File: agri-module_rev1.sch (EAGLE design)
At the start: 0 parts

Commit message: add ISL and new RJ45 pinout
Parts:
- added C1, C2: 100nF, BrainGrid - Capacitors:C_100N_0402
- added LED1, LED2, LED3: (no value), BrainGrid - Diodes:LEDCHIPLED-0603-TTW
- added R1, R2: 1.8k, BrainGrid - Resistors:R_1.8K_0402
- added U$1: RJ45_RA_SMD, BrainGrid - Electromechanical:RJ45_RA_SMD
- added U$2: RJ45_OUT_AGRI-BRD, BrainGrid - Electromechanical:RJ45_OUT_AGRI-BRD
- added U$3: BME280, BrainGrid - Sensors:BME280
- added U$4: ADS1015, BrainGrid - Analog:ADS1015
- added U$5: ISL29125_RGB_SENSE, BrainGrid - Sensors:ISL29125_RGB_SENSE
- added U$6: PCA9540B_I2C_SWITCH, NXP:PCA9540B_I2C_SWITCH
- added U1: 74HC1G79GW, NXP:74HC1G79GW
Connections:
- new net 3.6V_HP: C1.1, C2.1, R1.2, R2.2, U$1.+5V', U$3.CSB, U$3.VCC, U$3.VREF, U$4.ADDR, U$4.VCC, U$6.VCC
- new net 5V: U$1.+5V, U$2.+5V
- new net GND: LED1.C, LED2.C, LED3.C, U$1.GND, U$2.GND, U$3.GND1, U$4.GND, U$6.GND
- new net N$1: R1.1, U$3.SDI
- new net N$10: U$1.GND'
- new net N$11: U$1.SDA, U$6.SDA
- new net N$12: U$3.SDO, U$4.SDA, U$5.SDA, U$6.D0
- new net N$13: U$3.SCK, U$4.SCL, U$5.SCL, U$6.C0
- new net N$14: C1.2, C2.2, U$3.GND2
- new net N$2: R2.1
- new net N$3: U$1.SCL, U$6.SCL
- new net N$4: U$4.CH0
- new net N$5: LED3.A, U$4.CH1
- new net N$6: LED2.A, U$4.CH2
- new net N$7: LED1.A, U$4.CH3
- new net N$8: U$6.C1
- new net N$9: U$6.D1
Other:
- note added: "ADD CO2"
- note added: "ADD PULLUPS"
- note added: "CHAIN DIRECTION"
- note added: "Spectra ADC"

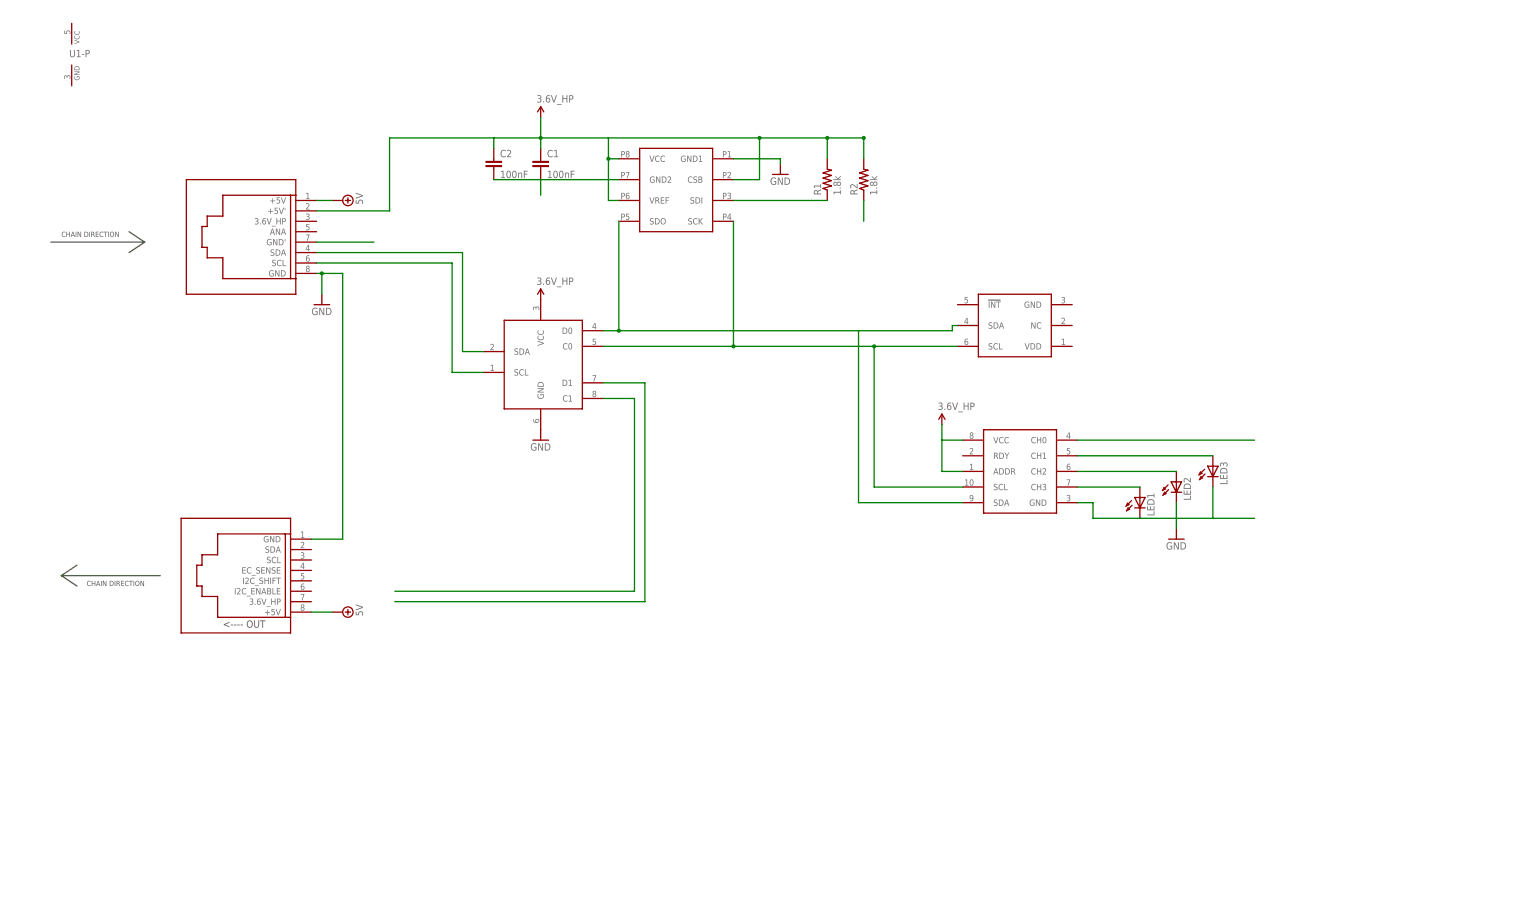
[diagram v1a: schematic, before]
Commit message: Everything wired up, not looked over yet
-replaced ISL with RGB gesture
-added hot film amp and CO2 amp
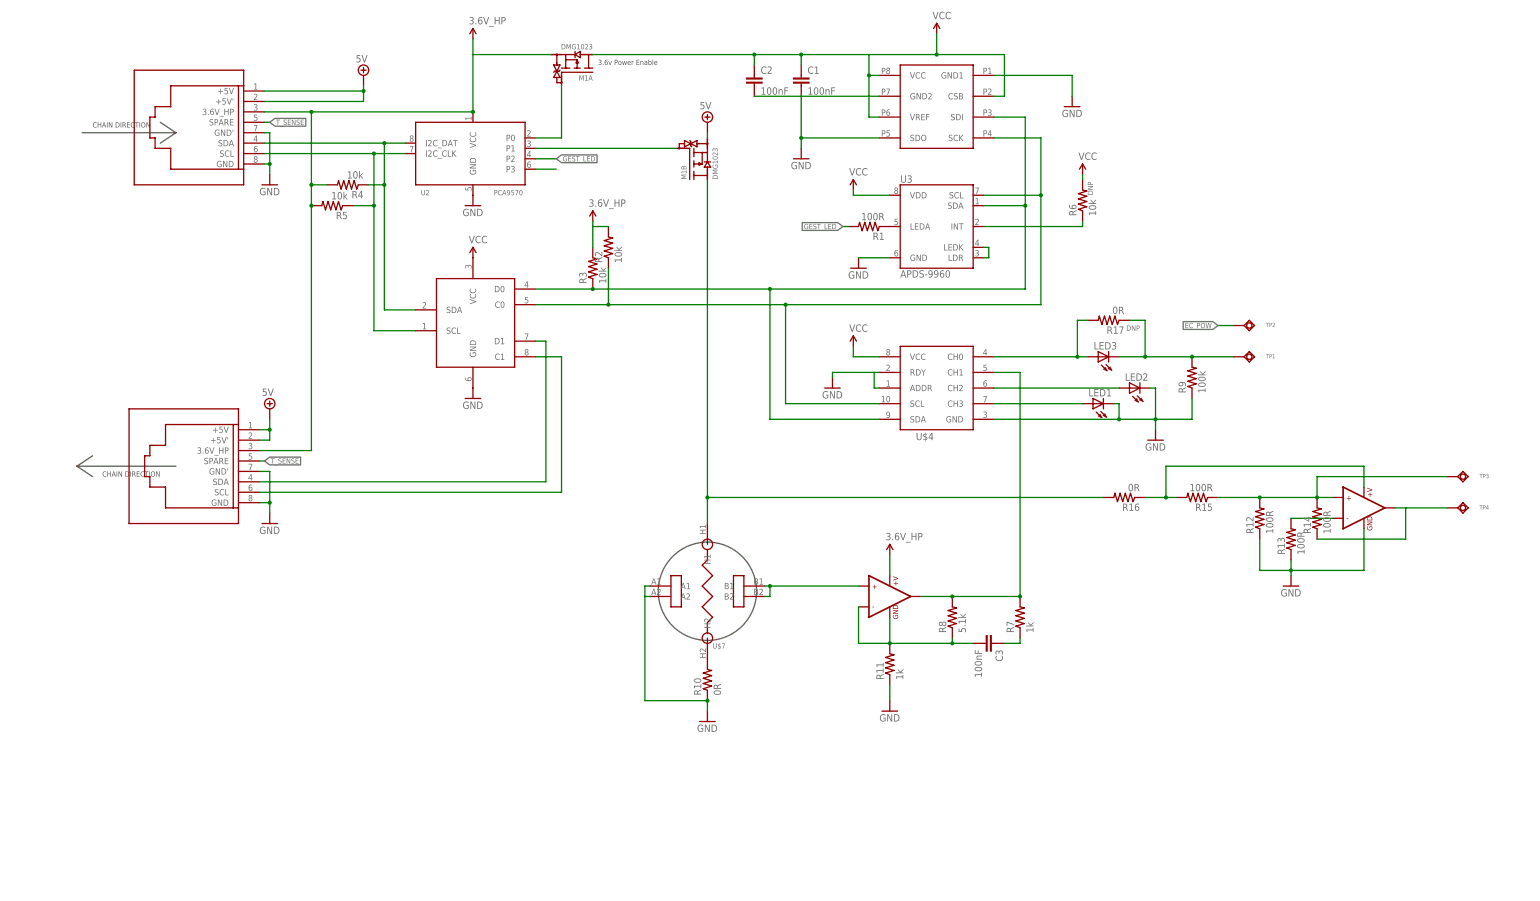
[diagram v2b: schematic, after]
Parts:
- removed U1: 74HC1G79GW, NXP:74HC1G79GW
- added C3: 100nF, BrainGrid - Capacitors:C_100N_0402
- added M1: DMG1023, BrainGrid - Transistors:DMG1023
- added R10, R16, R17: 0R, BrainGrid - Resistors:R_0R_0402
- added R11, R7: 1k, BrainGrid - Resistors:R_1K_0402
- added R12, R13, R14, R15: 100R, BrainGrid - Resistors:R_100R_0402
- added R3, R4, R5, R6: 10k, BrainGrid - Resistors:R_10K_0402
- added R8: 5.1k, BrainGrid - Resistors:R_5.1K_0402
- added R9: 100k, BrainGrid - Resistors:R_100K_0402
- added TP1, TP2, TP3, TP4: TEST_PAD, BrainGrid - Electromechanical:TEST_PAD
- added U$7: MG811, BrainGrid - Sensors:MG811
- added U$8: MCP6001T, SparkFun-AnalogIC:MCP6001T
- added U2: PCA9570, BrainGrid - MAC-PHY-Glue:PCA9570
- added U3: APDS-9960, BrainGrid - Sensors:APDS-9960
- R1: value 1.8k -> 100R; device BrainGrid - Resistors:R_1.8K_0402 -> BrainGrid - Resistors:R_100R_0402
- R2: value 1.8k -> 10k; device BrainGrid - Resistors:R_1.8K_0402 -> BrainGrid - Resistors:R_10K_0402
- U$2: value RJ45_OUT_AGRI-BRD -> RJ45_RA_SMD; device BrainGrid - Electromechanical:RJ45_OUT_AGRI-BRD -> BrainGrid - Electromechanical:RJ45_RA_SMD
- U$5: value ISL29125_RGB_SENSE -> MCP6001T; device BrainGrid - Sensors:ISL29125_RGB_SENSE -> SparkFun-AnalogIC:MCP6001T
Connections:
- removed net N$5 (its old number): LED3.A, U$4.CH1
- new net CO2_POW: M1B.D2, R16.2, U$7.H1
- new net EC_POW: TP2.TP, U2.P3
- new net GEST_LED: R1.2, U2.P2
- new net N$15: R5.1, U$1.SCL, U$6.SCL, U2.I2C_CLK
- new net N$16: R7.2, R8.2, U$4.CH1, U$5.OUT1
- new net N$17: R10.2, U$7.H2
- new net N$18: M1B.G2, U2.P1
- new net N$19: C3.1, R7.1
- new net N$20: R13.2, U$8.-IN1
- new net N$21: R12.2, R14.2, R15.1, TP3.TP, U$8.+IN1
- new net N$22: R14.1, TP4.TP, U$8.OUT1
- new net N$23: R15.2, R16.1, U$8.+V
- new net N$24: LED3.A, R17.2, U$4.CH0
- new net N$7: U$2.SDA, U$6.D1
- new net T_SENSE: U$1.SPARE, U$2.SPARE
- new net VCC: C1.1, C2.1, M1A.D2, R6.2, U$3.CSB, U$3.VCC, U$3.VREF, U$4.VCC, U$6.VCC, U3.VDD
- net 3.6V_HP: now also M1A.S2, R3.2, R4.2, R5.2, U$1.3.6V_HP, U$2.3.6V_HP, U$5.+V, U2.VCC; no longer C1.1, C2.1, R1.2, U$1.+5V', U$3.CSB, U$3.VCC, U$3.VREF, U$4.ADDR, U$4.VCC, U$6.VCC
- net 5V: now also M1B.S2, U$1.+5V', U$2.+5V'
- net GND: now also C1.2, C2.2, R10.1, R11.1, R12.1, R13.1, R9.1, U$1.GND', U$2.GND', U$3.GND2, U$3.SDO, U$4.ADDR, U$4.RDY, U$7.A1, U$7.A2, U$8.GND, U2.GND, U3.GND; no longer LED3.C
- net N$1: now also M1A.G2, U2.P0; no longer R1.1, U$3.SDI
- net N$10: now also R6.1, U3.INT; no longer U$1.GND'
- net N$11: now also R3.1, U$3.SDI, U$4.SDA, U$6.D0, U3.SDA; no longer U$1.SDA, U$6.SDA
- net N$12: now also LED3.C, R17.1, R9.2, TP1.TP; no longer U$3.SDO, U$4.SDA, U$5.SDA, U$6.D0
- net N$13: now also C3.2, R11.2, R8.1, U$5.-IN1, U$5.GND; no longer U$3.SCK, U$4.SCL, U$5.SCL, U$6.C0
- net N$14: now also R4.1, U$1.SDA, U$6.SDA, U2.I2C_DAT; no longer C1.2, C2.2, U$3.GND2
- net N$2: now also U3.LDR, U3.LEDK; no longer R2.1
- net N$3: now also R2.1, U$3.SCK, U$4.SCL, U$6.C0, U3.SCL; no longer U$1.SCL, U$6.SCL
- net N$4: now also R1.1, U3.LEDA; no longer U$4.CH0
- net N$8: now also U$2.SCL
- net N$9: now also U$5.+IN1, U$7.B1, U$7.B2; no longer U$6.D1
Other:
- note added: "3.6v Power Enable"
- note added: "adc-Mplex"
- note added: "check val"
- note added: "check vals"
- note added: "hot film"
- note added: "spectra i2c / gesture"
- note added: "temp/press/ humidity"
- note removed: "ADD CO2"
- note removed: "ADD PULLUPS"
- note removed: "Spectra ADC"
- moved on the sheet: C1, C2, LED1, LED2, LED3, R1, R2

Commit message: Added indication use for one of LEDs
-also connected EC_pow correctly
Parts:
- added D1: DB2S205, EAP - Library:DB2S205
- added R18: 10k, BrainGrid - Resistors:R_10K_0402
- added R19: 100R, BrainGrid - Resistors:R_100R_0402
- R1: value 100R -> 10k; device BrainGrid - Resistors:R_100R_0402 -> BrainGrid - Resistors:R_10K_0402
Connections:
- removed net N$6: LED2.A, U$4.CH2
- new net LED_INDICATE: D1.C, LED2.A, U$4.CH2
- net 3.6V_HP: now also R1.1, R18.1
- net GEST_LED: now also R19.2, U3.LEDA; no longer R1.2
- net N$4: now also D1.A, R19.1; no longer R1.1, U3.LEDA
- net N$7: now also R18.2
- net N$8: now also R1.2
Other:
- note removed: "check val"
- note removed: "check vals"
- moved on the sheet: R1
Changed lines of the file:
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@@
 <part name="GND4" library="BrainGrid - Supplies" deviceset="GND" device=""/>
 <part name="GND6" library="BrainGrid - Supplies" deviceset="GND" device=""/>
-<part name="R1" library="BrainGrid - Resistors" deviceset="R_100R" device="_0402" value="100R"/>
 <part name="R3" library="BrainGrid - Resistors" deviceset="R_10K" device="_0402" value="10k"/>
 <part name="SUPPLY2" library="BrainGrid - Supplies" deviceset="3.6V_HP" device=""/>
@@
 <attribute name="POPULATE" value="DNP"/>
 </part>
+<part name="R19" library="BrainGrid - Resistors" deviceset="R_100R" device="_0402" value="100R">
+<attribute name="POPULATE" value="DNP"/>
+</part>
+<part name="D1" library="EAP - Library" deviceset="DB2S205" device="">
+<attribute name="POPULATE" value="DNP"/>
+</part>
+<part name="R1" library="BrainGrid - Resistors" deviceset="R_10K" device="_0402" value="10k"/>
+<part name="R18" library="BrainGrid - Resistors" deviceset="R_10K" device="_0402" value="10k"/>
 </parts>
 <sheets>
@@
 <wire x1="26.67" y1="115.57" x2="30.48" y2="118.11" width="0.1524" layer="97"/>
 <text x="46.99" y="114.3" size="1.27" layer="97" rot="R180">CHAIN DIRECTION</text>
-<text x="210.82" y="176.53" size="1.27" layer="134">check val</text>
 <text x="229.87" y="176.53" size="0.8128" layer="90">spectra i2c
   / gesture</text>
@@
 humidity</text>
 <text x="233.68" y="128.27" size="0.8128" layer="90">adc-Mplex</text>
-<text x="157.48" y="162.56" size="1.27" layer="134">check vals</text>
-<text x="93.98" y="176.53" size="1.27" layer="134">check vals</text>
 <text x="356.87" y="107.95" size="1.27" layer="90">hot film</text>
 </plain>
@@
 <instance part="GND4" gate="G$1" x="123.19" y="132.08"/>
 <instance part="GND6" gate="G$1" x="123.19" y="179.07"/>
-<instance part="R1" gate="G$1" x="219.71" y="173.99" rot="R180"/>
 <instance part="R3" gate="G$1" x="152.4" y="163.83" rot="R90"/>
 <instance part="SUPPLY2" gate="G$1" x="152.4" y="175.26"/>
@@
 <attribute name="POPULATE" x="285.75" y="149.86" size="1.27" layer="96" rot="R180"/>
 </instance>
+<instance part="R19" gate="G$1" x="257.81" y="147.32" rot="R180">
+<attribute name="POPULATE" x="256.54" y="146.05" size="1.27" layer="96" rot="R180"/>
+</instance>
+<instance part="D1" gate="D" x="264.16" y="138.43" rot="R270">
+<attribute name="POPULATE" x="265.43" y="139.7" size="1.27" layer="96" rot="R270"/>
+</instance>
+<instance part="R1" gate="G$1" x="96.52" y="114.3" rot="R270"/>
+<instance part="R18" gate="G$1" x="104.14" y="116.84" rot="R270"/>
 </instances>
 <busses>
@@
 <pinref part="U$2" gate="G$1" pin="3.6V_HP"/>
 <wire x1="71.12" y1="119.38" x2="83.82" y2="119.38" width="0.1524" layer="91"/>
-<wire x1="83.82" y1="119.38" x2="83.82" y2="179.07" width="0.1524" layer="91"/>
 <junction x="83.82" y="179.07"/>
 <pinref part="SUPPLY1" gate="G$1" pin="3.6V_HP"/>
+<wire x1="83.82" y1="119.38" x2="83.82" y2="127" width="0.1524" layer="91"/>
+<wire x1="83.82" y1="127" x2="83.82" y2="179.07" width="0.1524" layer="91"/>
 <wire x1="123.19" y1="215.9" x2="123.19" y2="219.71" width="0.1524" layer="91"/>
+<pinref part="R18" gate="G$1" pin="1"/>
+<wire x1="96.52" y1="121.92" x2="100.33" y2="121.92" width="0.1524" layer="91"/>
+<pinref part="R1" gate="G$1" pin="1"/>
+<wire x1="100.33" y1="121.92" x2="104.14" y2="121.92" width="0.1524" layer="91"/>
+<wire x1="96.52" y1="119.38" x2="96.52" y2="121.92" width="0.1524" layer="91"/>
+<wire x1="100.33" y1="121.92" x2="100.33" y2="127" width="0.1524" layer="91"/>
+<wire x1="100.33" y1="127" x2="83.82" y2="127" width="0.1524" layer="91"/>
+<junction x="83.82" y="127"/>
 </segment>
 <segment>
@@
 <net name="EC_POW" class="0">
 <segment>
-<pinref part="U2" gate="G$1" pin="P3"/>
-<wire x1="138.43" y1="187.96" x2="143.51" y2="187.96" width="0.1524" layer="91"/>
-</segment>
-<segment>
 <pinref part="TP2" gate="TP" pin="TP"/>
 <wire x1="308.61" y1="149.86" x2="304.8" y2="149.86" width="0.1524" layer="91"/>
 <label x="304.8" y="149.86" size="1.27" layer="95" rot="R180" xref="yes"/>
+</segment>
+<segment>
+<pinref part="U2" gate="G$1" pin="P3"/>
+<wire x1="138.43" y1="187.96" x2="143.51" y2="187.96" width="0.1524" layer="91"/>
+<label x="143.51" y="187.96" size="1.27" layer="95" xref="yes"/>
 </segment>
 </net>
@@
 </segment>
 </net>
-<net name="N$4" class="0">
-<segment>
-<pinref part="U3" gate="U" pin="LEDA"/>
-<pinref part="R1" gate="G$1" pin="1"/>
-</segment>
-</net>
 <net name="N$5" class="0">
 <segment>
@@
 </segment>
 </net>
-<net name="N$6" class="0">
+<net name="LED_INDICATE" class="0">
 <segment>
 <pinref part="U$4" gate="G$1" pin="CH2"/>
 <pinref part="LED2" gate="G$1" pin="A"/>
-<wire x1="250.19" y1="134.62" x2="280.67" y2="134.62" width="0.1524" layer="91"/>
+<wire x1="250.19" y1="134.62" x2="264.16" y2="134.62" width="0.1524" layer="91"/>
+<pinref part="D1" gate="D" pin="C"/>
+<wire x1="264.16" y1="134.62" x2="280.67" y2="134.62" width="0.1524" layer="91"/>
+<wire x1="264.16" y1="135.89" x2="264.16" y2="134.62" width="0.1524" layer="91"/>
+<junction x="264.16" y="134.62"/>
 </segment>
 </net>
@@
 <pinref part="U$2" gate="G$1" pin="SCL"/>
 <pinref part="U$6" gate="G$1" pin="C1"/>
-<wire x1="144.78" y1="109.22" x2="71.12" y2="109.22" width="0.1524" layer="91"/>
+<wire x1="144.78" y1="109.22" x2="96.52" y2="109.22" width="0.1524" layer="91"/>
+<wire x1="96.52" y1="109.22" x2="71.12" y2="109.22" width="0.1524" layer="91"/>
 <wire x1="138.43" y1="142.24" x2="144.78" y2="142.24" width="0.1524" layer="91"/>
 <wire x1="144.78" y1="142.24" x2="144.78" y2="109.22" width="0.1524" layer="91"/>
+<pinref part="R1" gate="G$1" pin="2"/>
+<junction x="96.52" y="109.22"/>
 </segment>
 </net>
@@
 <wire x1="140.97" y1="146.05" x2="140.97" y2="111.76" width="0.1524" layer="91"/>
 <pinref part="U$2" gate="G$1" pin="SDA"/>
-<wire x1="140.97" y1="111.76" x2="71.12" y2="111.76" width="0.1524" layer="91"/>
+<wire x1="140.97" y1="111.76" x2="104.14" y2="111.76" width="0.1524" layer="91"/>
+<pinref part="R18" gate="G$1" pin="2"/>
+<wire x1="104.14" y1="111.76" x2="71.12" y2="111.76" width="0.1524" layer="91"/>
+<junction x="104.14" y="111.76"/>
 </segment>
 </net>
@@
 </segment>
 <segment>
-<pinref part="R1" gate="G$1" pin="2"/>
-<wire x1="214.63" y1="173.99" x2="213.36" y2="173.99" width="0.1524" layer="91"/>
 <label x="213.36" y="173.99" size="1.27" layer="95" rot="R180" xref="yes"/>
+<pinref part="U3" gate="U" pin="LEDA"/>
+<wire x1="213.36" y1="173.99" x2="224.79" y2="173.99" width="0.1524" layer="91"/>
+</segment>
+<segment>
+<wire x1="252.73" y1="147.32" x2="251.46" y2="147.32" width="0.1524" layer="91"/>
+<label x="251.46" y="147.32" size="1.27" layer="95" rot="R180" xref="yes"/>
+<pinref part="R19" gate="G$1" pin="2"/>
 </segment>
 </net>
@@
 </segment>
 </net>
+<net name="N$4" class="0">
+<segment>
+<wire x1="264.16" y1="147.32" x2="262.89" y2="147.32" width="0.1524" layer="91"/>
+<pinref part="R19" gate="G$1" pin="1"/>
+<pinref part="D1" gate="D" pin="A"/>
+<wire x1="264.16" y1="147.32" x2="264.16" y2="140.97" width="0.1524" layer="91"/>
+</segment>
+</net>

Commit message: Added name
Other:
- note added: "James Hutton"
- note added: "Rev 1"
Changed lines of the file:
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@@
 <text x="233.68" y="128.27" size="0.8128" layer="90">adc-Mplex</text>
 <text x="356.87" y="107.95" size="1.27" layer="90">hot film</text>
+<text x="328.93" y="5.08" size="2.286" layer="90">James Hutton</text>
+<text x="326.39" y="15.24" size="1.778" layer="90">Rev 1</text>
 </plain>
 <instances>

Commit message: Initial Board Layout
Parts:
- removed TP1, TP2: TEST_PAD, BrainGrid - Electromechanical:TEST_PAD
- U$2: value RJ45_RA_SMD -> 35RASMT2BHNTRX; device BrainGrid - Electromechanical:RJ45_RA_SMD -> BrainGrid - Electromechanical:35RASMT2BHNTRX
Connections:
- removed net N$12: LED3.C, R17.1, R9.2, TP1.TP
- new net EC_SENSE: LED3.C, R17.1, R9.2, U$2.1
- net 3.6V_HP: now also C1.1; no longer U$2.3.6V_HP
- net 5V: no longer U$2.+5V, U$2.+5V'
- net EC_POW: now also U$2.4; no longer TP2.TP
- net GND: now also U$2.5; no longer U$2.GND, U$2.GND'
- net N$7: no longer U$2.SDA
- net N$8: no longer U$2.SCL
- net T_SENSE: no longer U$2.SPARE
- net VCC: no longer C1.1
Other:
- moved on the sheet: C1, C2
